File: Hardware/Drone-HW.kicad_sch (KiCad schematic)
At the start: 39 parts, among them Con5 espTool_conn, J2 Conn_01x02_Socket, J3 Conn_01x02_Socket, J4 Conn_01x02_Socket, J5 Conn_01x02_Socket, Q1 AO3400A, Q2 AO3400A, Q3 AO3400A, Q4 AO3400A, Q5 BC846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

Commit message: Adicionando sybols e footprint dos escs e symbol do stepdown
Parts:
- removed D1, D2, D3, D5: SS33, Diode_SMD:D_SMA, symbol Diode:SS33
- removed J2, J3, J4, J5: Conn_01x02_Socket, Connector_PinHeader_1.00mm:PinHeader_1x02_P1.00mm_Vertical, symbol Connector:Conn_01x02_Socket
- removed Q1, Q2, Q3, Q4: AO3400A, Package_TO_SOT_SMD:SOT-23, symbol Transistor_FET:AO3400A
- removed R1, R2, R3, R4: 470, Local_Resistor_SMD:R_0805_2012Metric_Pad1.15x1.40mm_HandSolder, symbol Local_resistors:3k3
- removed R5, R6, R7, R8: 10k, Local_Resistor_SMD:R_0805_2012Metric_Pad1.15x1.40mm_HandSolder, symbol Local_resistors:3k3
- added BrushlessMotor1: B1, MPU-6050_Module:BrushlessMotorDriver_MODULE, symbol MPU6050_module:BrushlessMotor_MODULE
- added BrushlessMotor2: B2, MPU-6050_Module:BrushlessMotorDriver_MODULE, symbol MPU6050_module:BrushlessMotor_MODULE
- added BrushlessMotor3: B3, MPU-6050_Module:BrushlessMotorDriver_MODULE, symbol MPU6050_module:BrushlessMotor_MODULE
- added BrushlessMotor4: B4, MPU-6050_Module:BrushlessMotorDriver_MODULE, symbol MPU6050_module:BrushlessMotor_MODULE
- added J1, J2, J3, J4: Conn_01x03_Socket, Connector_PinHeader_1.00mm:PinHeader_1x03_P1.00mm_Vertical, symbol Connector:Conn_01x03_Socket
- added J5: Conn_01x02_Pin, symbol Connector:Conn_01x02_Pin
- added STEP_DOWN1: STEPDOWN_23V_3V3, symbol MPU6050_module:STEPDOWN_3V3
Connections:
- net +3V3: now also STEP_DOWN1.3 (+OUT)
- net +7V4: now also BrushlessMotor1.4 (M_VCC), BrushlessMotor2.4 (M_VCC), BrushlessMotor3.4 (M_VCC), BrushlessMotor4.4 (M_VCC), J5.1 (Pin_1), STEP_DOWN1.1 (+IN)
- net GND: now also BrushlessMotor1.3 (REF_PWM), BrushlessMotor2.3 (REF_PWM), BrushlessMotor3.3 (REF_PWM), BrushlessMotor4.3 (REF_PWM), STEP_DOWN1.4 (-OUT)
- net Motor1: now also BrushlessMotor1.2 (PWM)
- net Motor2: now also BrushlessMotor2.2 (PWM)
- net Motor3: now also BrushlessMotor3.2 (PWM)
- net Motor4: now also BrushlessMotor4.2 (PWM)
- new net: BrushlessMotor2.5 (M1), J2.1 (Pin_1)
- new net: BrushlessMotor2.6 (M2), J2.2 (Pin_2)
- new net: BrushlessMotor2.7 (M3), J2.3 (Pin_3)
- new net: BrushlessMotor3.5 (M1), J3.1 (Pin_1)
- new net: BrushlessMotor3.6 (M2), J3.2 (Pin_2)
- new net: BrushlessMotor3.7 (M3), J3.3 (Pin_3)
- new net: BrushlessMotor1.5 (M1), J1.1 (Pin_1)
- new net: BrushlessMotor1.6 (M2), J1.2 (Pin_2)
- new net: BrushlessMotor1.7 (M3), J1.3 (Pin_3)
- new net: BrushlessMotor4.5 (M1), J4.1 (Pin_1)
- new net: BrushlessMotor4.6 (M2), J4.2 (Pin_2)
- new net: BrushlessMotor4.7 (M3), J4.3 (Pin_3)
- new net GND_7V4: BrushlessMotor1.1 (M_GND), BrushlessMotor2.1 (M_GND), BrushlessMotor3.1 (M_GND), BrushlessMotor4.1 (M_GND), J5.2 (Pin_2), STEP_DOWN1.2 (-IN)

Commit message: hardware arrumado, retirando escs da pcb e diminuindo tamanho
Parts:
- removed J1, J2, J3, J4: Conn_01x03_Socket, Connector_PinHeader_1.00mm:PinHeader_1x03_P1.00mm_Vertical, symbol Connector:Conn_01x03_Socket
- added J1, J2, J3, J4: Conn_01x01_Pin, Connector_PinHeader_2.54mm:PinHeader_1x01_P2.54mm_Vertical, symbol Connector:Conn_01x01_Pin
- added U3: NRF24L01_Breakout, RF_Module:nRF24L01_Breakout, symbol RF:NRF24L01_Breakout
- BrushlessMotor1, BrushlessMotor2, BrushlessMotor3, BrushlessMotor4: footprint MPU-6050_Module:BrushlessMotorDriver_MODULE -> (none)
- J5: footprint (none) -> Connector_PinHeader_2.54mm:PinHeader_1x02_P2.54mm_Vertical
- STEP_DOWN1: footprint (none) -> MPU-6050_Module:StepDown3v3_Module
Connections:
- net +3V3: now also U2.7 (ADO), U3.2 (VCC)
- net +7V4: no longer BrushlessMotor1.4 (M_VCC), BrushlessMotor2.4 (M_VCC), BrushlessMotor3.4 (M_VCC), BrushlessMotor4.4 (M_VCC)
- net B_START: now also U1.12 (IO27); no longer U1.6 (IO34_(IN))
- net GND: now also U3.1 (GND)
- net GND_7V4: no longer BrushlessMotor1.1 (M_GND), BrushlessMotor2.1 (M_GND), BrushlessMotor3.1 (M_GND), BrushlessMotor4.1 (M_GND)
- net Motor1: now also J1.1 (Pin_1)
- net Motor2: now also U1.26 (IO4), J2.1 (Pin_1); no longer U1.28 (IO17)
- net Motor3: now also U1.16 (IO13), J3.1 (Pin_1); no longer U1.30 (IO18)
- net Motor4: now also U1.13 (IO14), J4.1 (Pin_1); no longer U1.31 (IO19)
- net A_M2: now reaches BrushlessMotor2.5 (M1)
- net B_M2: now reaches BrushlessMotor2.6 (M2)
- net C_M2: now reaches BrushlessMotor2.7 (M3)
- net A_M3: now reaches BrushlessMotor3.5 (M1)
- net B_M3: now reaches BrushlessMotor3.6 (M2)
- net C_M3: now reaches BrushlessMotor3.7 (M3)
- net A_M1: now reaches BrushlessMotor1.5 (M1)
- net B_M1: now reaches BrushlessMotor1.6 (M2)
- net C_M1: now reaches BrushlessMotor1.7 (M3)
- net MOSI: now reaches U1.37 (IO23)
- net MOSI: now also U3.6 (MOSI)
- net IRQ: now reaches U1.7 (IO35_(IN))
- net IRQ: now also U3.8 (IRQ)
- net CE: now reaches U1.8 (IO32)
- net CE: now also U3.3 (CE)
- net ~{CSN}: now reaches U1.9 (IO33)
- net ~{CSN}: now also U3.4 (~{CSN})
- net A_M4: now reaches BrushlessMotor4.5 (M1)
- net B_M4: now reaches BrushlessMotor4.6 (M2)
- net C_M4: now reaches BrushlessMotor4.7 (M3)
- net INT: now reaches U2.8 (INT)
- net INT: now also U1.6 (IO34_(IN))
- new net MISO: U1.31 (IO19), U3.7 (MISO)
- new net SCK: U1.30 (IO18), U3.5 (SCK)
- no-connect marks 26 -> 25
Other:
- note added: "A trilhas de alimentação do motor serão conectadas por jumpers externos. (M_VCC e M_GND)"
- moved on the sheet: BrushlessMotor1, BrushlessMotor2, BrushlessMotor3, BrushlessMotor4, C1, C2, C3

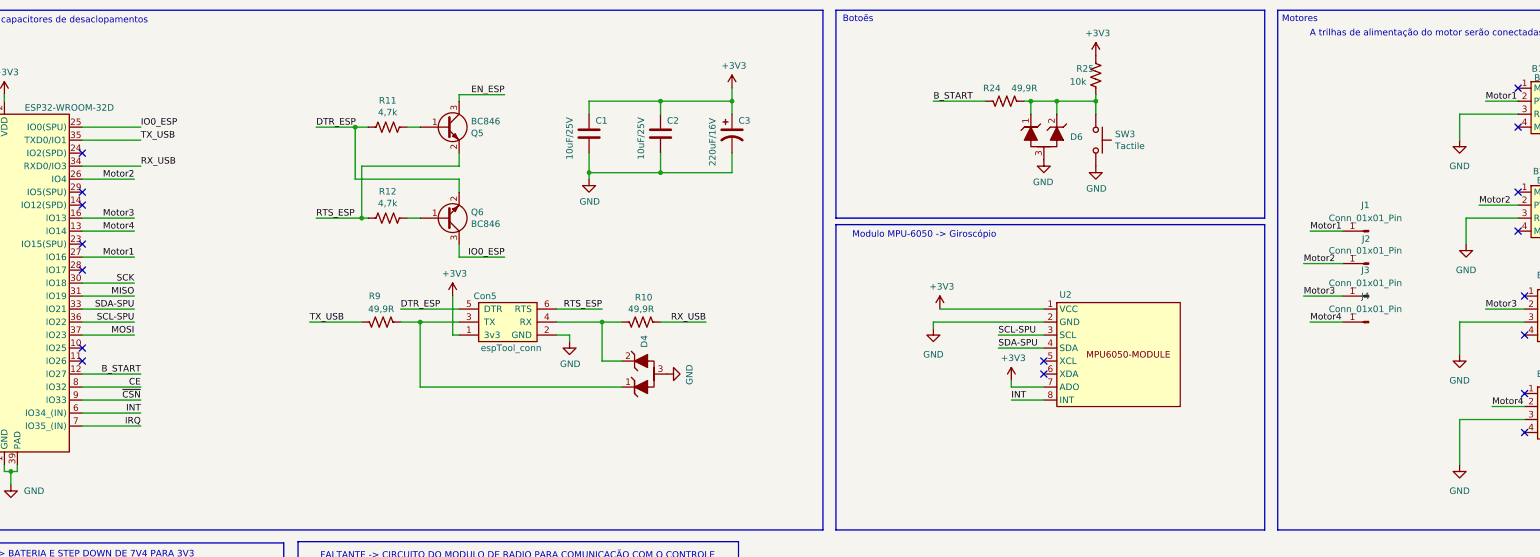
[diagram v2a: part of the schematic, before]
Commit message: Retirando modulos escs da pcb
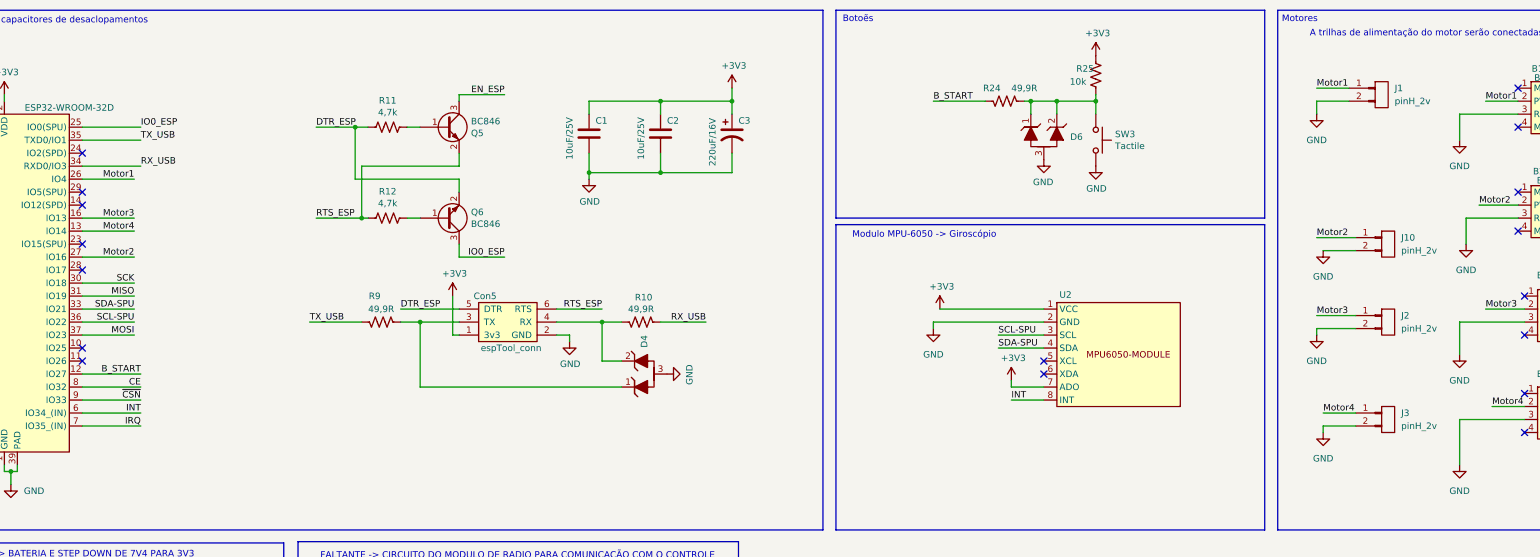
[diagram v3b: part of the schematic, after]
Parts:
- removed J1, J2, J3, J4: Conn_01x01_Pin, Connector_PinHeader_2.54mm:PinHeader_1x01_P2.54mm_Vertical, symbol Connector:Conn_01x01_Pin
- added J1, J10, J2, J3: pinH_2v, Local_Connector_PinHeader_2.54mm:PinHeader_1x02_P2.54mm_Vertical, symbol Local_connectors:pinH_2v
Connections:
- net GND: now also J1.2 (Pin_2), J10.2 (Pin_2), J2.2 (Pin_2), J3.2 (Pin_2)
- net Motor1: now also U1.26 (IO4), J1.1 (Pin_1); no longer U1.27 (IO16)
- net Motor2: now also U1.27 (IO16), J10.1 (Pin_1); no longer U1.26 (IO4)
- net Motor3: now also J2.1 (Pin_1)
- net Motor4: now also J3.1 (Pin_1)

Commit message: Finalizando hardware aguardando revisão
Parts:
- added D1: LED, Local_LED_THT:LED_D1.8mm_W3.3mm_H2.4mm, symbol Device:LED
- added R1: 10k, Local_Resistor_SMD:R_0805_2012Metric_Pad1.15x1.40mm_HandSolder, symbol Local_resistors:3k3
- added R2: 15k, Local_Resistor_SMD:R_0805_2012Metric_Pad1.15x1.40mm_HandSolder, symbol Local_resistors:3k3
- added R3: 330, Local_Resistor_SMD:R_0805_2012Metric_Pad1.15x1.40mm_HandSolder, symbol Local_resistors:3k3
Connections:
- net +7V4: now also R2.1
- net GND: now also D1.1 (K), R1.2
- net V_Bat: now reaches U1.11 (IO26)
- net V_Bat: now also R1.1, R2.2
- net at U1.28 (IO17): now also R3.2
- new net: D1.2 (A), R3.1
- no-connect marks 25 -> 23
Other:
- moved on the sheet: C1, C2, C3, Con5, D4, J5, Q5, Q6, R10, R11, R12, R9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

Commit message: Arrumando hardware
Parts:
- removed J1, J10, J2, J3: pinH_2v, Local_Connector_PinHeader_2.54mm:PinHeader_1x02_P2.54mm_Vertical, symbol Local_connectors:pinH_2v
- removed R3: 330, Local_Resistor_SMD:R_0805_2012Metric_Pad1.15x1.40mm_HandSolder, symbol Local_resistors:3k3
- added J1, J2, J3, J4: Conn_01x03, Connector_PinHeader_2.00mm:PinHeader_1x03_P2.00mm_Vertical, symbol Connector_Generic:Conn_01x03
- added R3: 470R, Local_Resistor_SMD:R_0805_2012Metric_Pad1.15x1.40mm_HandSolder, symbol Local_resistors:10k
- U1: footprint Local_RF_Module:ESP32-WROOM-32_PRODIGITAL -> RF_Module:ESP32-WROOM-32U
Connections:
- net +3V3: now also R3.1
- net GND: now also J1.2 (Pin_2), J2.2 (Pin_2), J3.2 (Pin_2), J4.2 (Pin_2); no longer D1.1 (K)
- net Motor1: now also J1.1 (Pin_1)
- net Motor2: now also J2.1 (Pin_1)
- net Motor3: now also J3.1 (Pin_1)
- net Motor4: now also J4.1 (Pin_1)
- net at D1.2 (A): now also R3.2
- net at U1.28 (IO17): now also D1.1 (K)
- net sw4: now reaches U1.10 (IO25)
- net sw4: now also J4.3 (Pin_3)
- net sw2: now reaches U1.14 (IO12(SPD))
- net sw2: now also J2.3 (Pin_3)
- net sw3: now reaches U1.23 (IO15(SPU))
- net sw3: now also J3.3 (Pin_3)
- net sw1: now reaches U1.29 (IO5(SPU))
- net sw1: now also J1.3 (Pin_3)
- no-connect marks 23 -> 19
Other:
- moved on the sheet: D1

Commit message: alteracoes finais
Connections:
- net +3V3: no longer Con5.1 (3v3)
- no-connect marks 19 -> 20
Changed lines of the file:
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@@
 	)
 	(no_connect
+		(at 144.78 80.01)
+	)
+	(no_connect
 		(at 260.35 82.55)
 	)
@@
 	(wire
 		(pts
-			(xy 143.51 80.01) (xy 143.51 72.39)
-		)
-		(stroke
-			(width 0)
-			(type default)
-		)
-	)
-	(wire
-		(pts
 			(xy 321.31 92.71) (xy 314.96 92.71)
 		)
@@
 	(wire
 		(pts
-			(xy 144.78 80.01) (xy 143.51 80.01)
-		)
-		(stroke
-			(width 0)
-			(type default)
-		)
-	)
-	(wire
-		(pts
 			(xy 31.75 34.29) (xy 31.75 36.83)
 		)
@@
 					(unit 1)
 				)
-			)
-		)
-	)
-	(symbol
-		(lib_id "Local_power:+3V3")
-		(at 143.51 72.39 0)
-		(unit 1)
-		(exclude_from_sim no)
-		(in_bom yes)
-		(on_board yes)
-		(dnp no)
-		(property "Reference" "#PWR011"
-			(at 143.51 76.2 0)
-			(effects
-				(font
-					(size 1.27 1.27)
-				)
-				(hide yes)
-			)
-		)
-		(property "Value" "+3V3"
-			(at 143.891 67.9958 0)
-			(effects
-				(font
-					(size 1.27 1.27)
-				)
-			)
-		)
-		(property "Footprint" ""
-			(at 143.51 72.39 0)
-			(effects
-				(font
-					(size 1.27 1.27)
-				)
-				(hide yes)
-			)
-		)
-		(property "Datasheet" ""
-			(at 143.51 72.39 0)
-			(effects
-				(font
-					(size 1.27 1.27)
-				)
-				(hide yes)
-			)
-		)
-		(property "Description" ""
-			(at 143.51 72.39 0)
-			(effects
-				(font
-					(size 1.27 1.27)
-				)
-				(hide yes)
-			)
-		)
-		(pin "1"
-		)
-		(instances
-			(project "Drone-HW"
-				(path "/01131552-7157-4f63-8aad-f62f04ef3457"
-					(reference "#PWR011")
-					(unit 1)
-				)

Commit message: Dando push na versão final de hardware
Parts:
- added H1, H2, H3, H4: MountingHole, MountingHole:MountingHole_2.1mm, symbol Mechanical:MountingHole
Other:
- note added: "CIRCUITO DE ALIMENTAÇÃO -> BATERIA E STEP DOWN DE 7V4 PARA 3V3"
- note added: "CIRCUITO DO MODULO DE RADIO PARA COMUNICAÇÃO COM O CONTROLE"
- note added: "FURO PLACA"
- note removed: "FALTA -> CIRCUITO DE ALIMENTAÇÃO -> BATERIA E STEP DOWN DE 7V4 PARA 3V3"
- note removed: "FALTANTE -> CIRCUITO DO MODULO DE RADIO PARA COMUNICAÇÃO COM O CONTROLE"
